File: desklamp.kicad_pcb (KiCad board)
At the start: 2 copper layers, 85.1 x 35.6 mm, 13 parts, among them J1 Power, J2 Neopixel, U1 itsy_bitsy

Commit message: Work on pcb and generate gerbers
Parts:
- RV0: value R_POT -> POT0
- RV1: value R_POT -> POT1
- RV2: value R_POT -> POT2
- RV3: value R_POT -> POT3
- moved U1 2.84 mm to (171.4, 115.6)
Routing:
- net +5V: track 109.8 -> 106.2 mm
- net Net-(RV1-Pad3): track 16.6 -> 19.7 mm
- net Net-(RV0-Pad3): track 31.6 -> 34.7 mm
- net Signal: track 27.5 -> 30.6 mm
- net GND: track 111.1 -> 114.2 mm, vias 1 -> 2
- net Net-(RV2-Pad3): track 6.35 -> 8.67 mm
- net Net-(RV3-Pad3): track 16.6 -> 14.6 mm

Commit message: Total PCB redesign
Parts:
- removed the REF** at (208.3, 123.2)
- removed the REF** at (208.3, 97.8)
- removed the REF** at (133.3, 97.8)
- added REF**: MountingHole_3.2mm_M3, MountingHole:MountingHole_3.2mm_M3, F.Cu at (204.5, 101.6)
- added REF**: MountingHole_3.2mm_M3, MountingHole:MountingHole_3.2mm_M3, F.Cu at (204.5, 73.7)
- added REF**: MountingHole_3.2mm_M3, MountingHole:MountingHole_3.2mm_M3, F.Cu at (154.9, 73.7)
- moved J2 50.6 mm to (172.7, 73.7), turned to 180 degrees
- moved U1 47.1 mm to (182.9, 69.8), turned to 0 degrees
- moved R1 35.1 mm to (179.1, 80.0), turned to 270 degrees
- moved RV0 33.5 mm to (154.9, 92.7), turned to 270 degrees
- moved C1 31.0 mm to (167.6, 91.4), turned to 90 degrees
- moved REF** 25.0 mm to (154.9, 110.5)
- moved J1 18.8 mm to (154.9, 81.3), turned to 270 degrees
- moved RV1 13.7 mm to (162.6, 110.5)
- moved RV3 13.7 mm to (195.6, 110.5)
- moved RV2 13.7 mm to (179.1, 110.5)
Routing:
- net GND: track 114.2 -> 0.00 mm, vias 2 -> 0
- net +5V: track 106.2 -> 0.00 mm
- net Net-(RV0-Pad3): track 34.7 -> 0.00 mm
- net Signal: track 30.6 -> 0.00 mm
- net Net-(J2-Pad2): track 25.7 -> 0.00 mm
- net Net-(RV1-Pad3): track 19.7 -> 0.00 mm
- net Net-(RV3-Pad3): track 14.6 -> 0.00 mm
- net Net-(RV2-Pad3): track 8.67 -> 0.00 mm
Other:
- board size 85.1 x 35.6 mm -> 59.7 x 47 mm

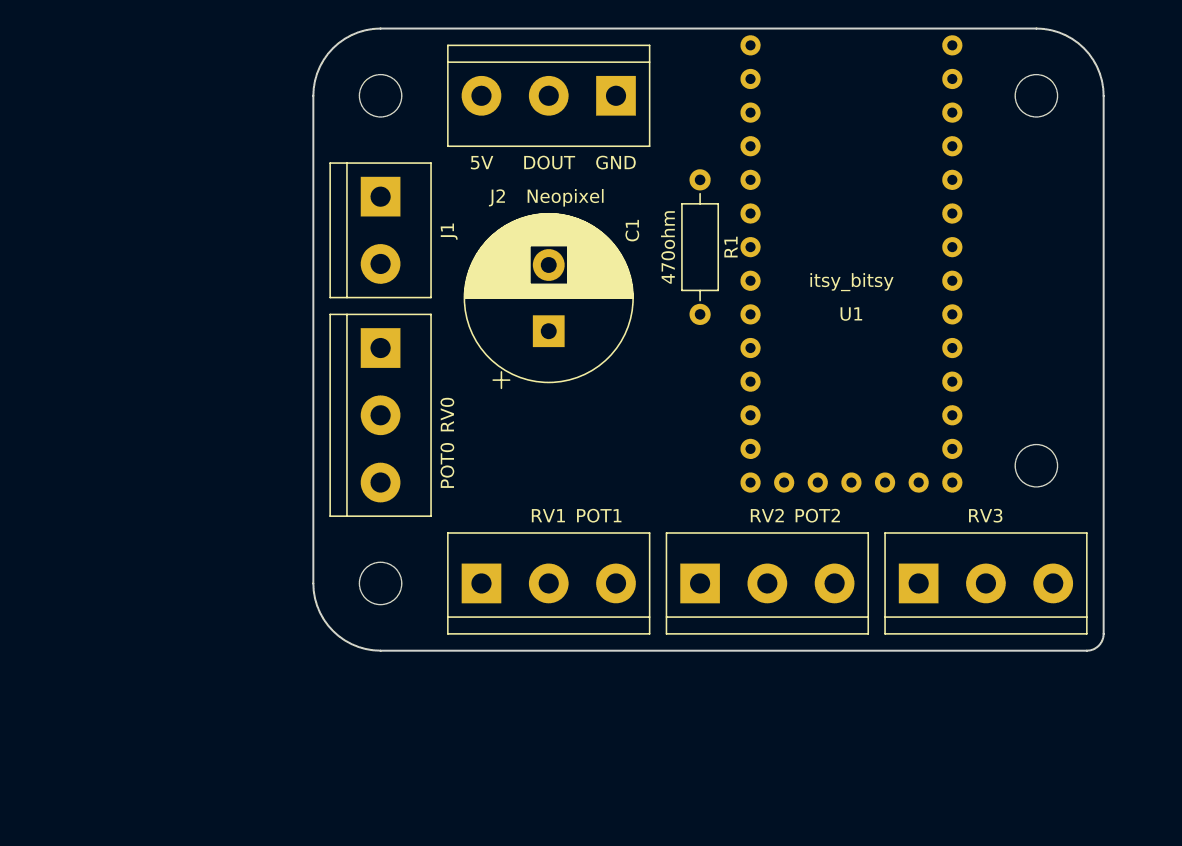
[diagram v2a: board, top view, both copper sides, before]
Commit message: Adjusted PCB and routed traces
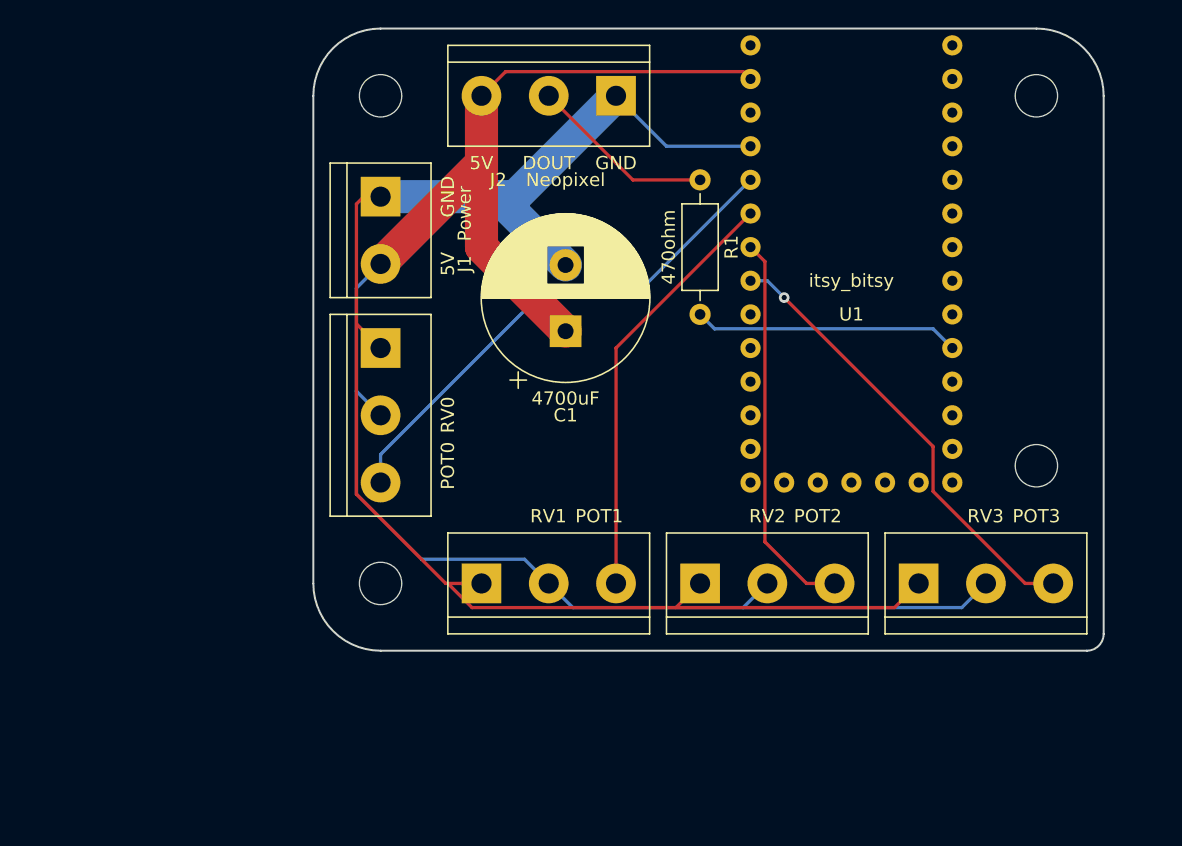
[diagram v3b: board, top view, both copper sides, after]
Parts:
- moved C1 1.27 mm to (168.9, 91.4)
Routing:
- net +5V: track 0.00 -> 127.6 mm
- net GND: track 0.00 -> 118.4 mm
- net Net-(RV0-Pad3): track 0.00 -> 38.7 mm
- net Net-(RV3-Pad3): track 0.00 -> 34.3 mm, vias 0 -> 1
- net Net-(RV1-Pad3): track 0.00 -> 32.1 mm
- net Net-(RV2-Pad3): track 0.00 -> 29.3 mm
- net Signal: track 0.00 -> 20.1 mm
- net Net-(J2-Pad2): track 0.00 -> 14.1 mm

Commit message: Moved some traces to front and added revision number
Rev 1.0
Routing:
- net Net-(RV0-Pad3): track 38.7 -> 37.7 mm
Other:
- board text added: "Rev 1.0"
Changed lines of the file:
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@@
   (general
     (thickness 1.6)
-    (drawings 8)
-    (tracks 61)
+    (drawings 9)
+    (tracks 60)
     (zones 0)
     (modules 13)
@@
       (net 30 "Net-(U1-Pad33)"))
   )
+  (gr_text "Rev 1.0" (at 204.47 87.63 90) (layer F.SilkS)
+    (effects (font (size 2 2) (thickness 0.45)))
+  )
   (gr_arc (start 208.28 114.3) (end 208.28 115.57) (angle -90) (layer Edge.Cuts) (width 0.15))
   (gr_arc (start 154.94 110.49) (end 149.86 110.49) (angle -90) (layer Edge.Cuts) (width 0.15))
@@
   (segment (start 193.754999 112.315001) (end 195.58 110.49) (width 0.25) (layer F.Cu) (net 3))
   (segment (start 177.244999 112.315001) (end 193.754999 112.315001) (width 0.25) (layer F.Cu) (net 3))
-  (segment (start 172.72 73.66) (end 176.53 77.47) (width 0.25) (layer B.Cu) (net 3))
-  (segment (start 176.53 77.47) (end 182.88 77.47) (width 0.25) (layer B.Cu) (net 3))
+  (segment (start 172.72 73.66) (end 176.53 77.47) (width 0.25) (layer F.Cu) (net 3))
+  (segment (start 176.53 77.47) (end 182.88 77.47) (width 0.25) (layer F.Cu) (net 3))
   (segment (start 196.667001 91.257001) (end 198.12 92.71) (width 0.25) (layer B.Cu) (net 4))
   (segment (start 180.157001 91.257001) (end 196.667001 91.257001) (width 0.25) (layer B.Cu) (net 4))
   (segment (start 179.07 90.17) (end 180.157001 91.257001) (width 0.25) (layer B.Cu) (net 4))
-  (segment (start 174.874991 88.015009) (end 182.88 80.01) (width 0.25) (layer B.Cu) (net 31))
-  (segment (start 167.673671 88.015009) (end 174.874991 88.015009) (width 0.25) (layer B.Cu) (net 31))
-  (segment (start 154.94 100.74868) (end 167.673671 88.015009) (width 0.25) (layer B.Cu) (net 31))
-  (segment (start 154.94 102.87) (end 154.94 100.74868) (width 0.25) (layer B.Cu) (net 31))
+  (segment (start 182.88 80.455002) (end 182.88 80.01) (width 0.25) (layer F.Cu) (net 31))
+  (segment (start 160.465002 102.87) (end 182.88 80.455002) (width 0.25) (layer F.Cu) (net 31))
+  (segment (start 154.94 102.87) (end 160.465002 102.87) (width 0.25) (layer F.Cu) (net 31))
   (segment (start 172.72 92.71) (end 182.88 82.55) (width 0.25) (layer F.Cu) (net 32))
   (segment (start 172.72 110.49) (end 172.72 92.71) (width 0.25) (layer F.Cu) (net 32))

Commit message: Added a jumper for POT3 so that it can be used as a second NeoPixel port
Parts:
- removed REF** (x4): MountingHole_3.2mm_M3, MountingHole:MountingHole_3.2mm_M3
- removed RV3: POT3, TerminalBlock:TerminalBlock_bornier-3_P5.08mm
- added J3: POT3, TerminalBlock:TerminalBlock_bornier-3_P5.08mm, F.Cu at (195.6, 110.5)
- added JP1: Pot3 Jumper, Jumper:SolderJumper-3_P1.3mm_Bridged12_Pad1.0x1.5mm_NumberLabels, B.Cu at (190.5, 83.8)
- added MH0: MountingHole, MountingHole:MountingHole_3.2mm_M3, F.Cu at (154.9, 73.7)
- added MH1: MountingHole, MountingHole:MountingHole_3.2mm_M3, F.Cu at (154.9, 110.5)
- added MH2: MountingHole, MountingHole:MountingHole_3.2mm_M3, F.Cu at (204.5, 73.7)
- added MH3: MountingHole, MountingHole:MountingHole_3.2mm_M3, F.Cu at (204.5, 101.6)
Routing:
- net Net-(J3-Pad1): track 0.00 -> 28.8 mm
- net Net-(JP1-Pad1): track 34.3 -> 7.90 mm, vias 1 -> 0
- net GND: track 118.4 -> 128.6 mm
- net Net-(JP1-Pad3): track 0.00 -> 8.04 mm
- net Signal: vias 0 -> 1
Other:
- board text added: "Rev 1.1"
- board text removed: "Rev 1.0"

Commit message: Move JP1
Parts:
- moved JP1 3.81 mm to (190.5, 87.6)
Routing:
- net Net-(J3-Pad1): track 28.8 -> 25.0 mm
- net Net-(JP1-Pad3): track 8.04 -> 6.32 mm
- net Net-(JP1-Pad1): track 7.90 -> 6.32 mm
